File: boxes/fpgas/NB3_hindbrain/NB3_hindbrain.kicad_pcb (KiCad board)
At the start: 2 copper layers, 55.9 x 22.9 mm, 29 parts, among them IC1 FPGA_ICE40UP5K-SG48I, IC2 NOR_Flash_W25Q32JVSSIQ, J1 MicroUSB_10103594-0001LF, J2 Conn_01x20_Male, J3 Conn_01x20_Male, U1 USBtoSPI_FT4232HL, U2 EEPROM_93LC56BT-I-OT, Y1 Osc_12MHz_ECS-2520MV-120-BN-TR

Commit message: NB£_hindbrain layout update
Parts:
- added C12: 100nF, Capacitor_SMD:C_0402_1005Metric, F.Cu at (123.2, 62.2)
- added C13: 4.7uF, Capacitor_SMD:C_0603_1608Metric, F.Cu at (107.0, 66.0)
- added C14: 10uF, Capacitor_SMD:C_0603_1608Metric, F.Cu at (111.1, 66.0)
- added C15: 10uF, Capacitor_SMD:C_0603_1608Metric, F.Cu at (111.1, 63.5)
- added C16: 100nF, Capacitor_SMD:C_0402_1005Metric, F.Cu at (117.4, 65.2)
- added C17: 100nF, Capacitor_SMD:C_0402_1005Metric, F.Cu at (114.5, 67.1)
- added C18: 3.3uF, Capacitor_SMD:C_0603_1608Metric, F.Cu at (107.0, 63.5)
- added C19: 100nF, Capacitor_SMD:C_0402_1005Metric, F.Cu at (114.5, 65.2)
- added C20: 100nF, Capacitor_SMD:C_0402_1005Metric, F.Cu at (120.3, 62.2)
- added C21: 10uF, Capacitor_SMD:C_0603_1608Metric, F.Cu at (115.5, 58.0)
- added C22: 10uF, Capacitor_SMD:C_0603_1608Metric, F.Cu at (115.1, 60.5)
- added C23: 100nF, Capacitor_SMD:C_0402_1005Metric, F.Cu at (121.4, 60.3)
- added C24: 100nF, Capacitor_SMD:C_0402_1005Metric, F.Cu at (117.4, 67.1)
- added C25: 4.7uF, Capacitor_SMD:C_0603_1608Metric, F.Cu at (111.1, 60.9)
- added C26: 100nF, Capacitor_SMD:C_0402_1005Metric, F.Cu at (120.3, 64.2)
- added C27: 4.7uF, Capacitor_SMD:C_0603_1608Metric, F.Cu at (119.5, 58.0)
- added C28: 100nF, Capacitor_SMD:C_0402_1005Metric, F.Cu at (124.3, 59.7)
- added D1: Diode_1N4148WS-7-F, NB3_hindbrain:Diode_1N4148WS-7-F, F.Cu at (107.3, 58.2)
- added FB1: FB_BLM18HE152SN1D, NB3_hindbrain:FB_BLM18HE152SN1D, F.Cu at (111.5, 58.0)
- added FB2: FB_BLM18HE152SN1D, NB3_hindbrain:FB_BLM18HE152SN1D, F.Cu at (107.1, 60.9)
- added R10: 10k, Resistor_SMD:R_0402_1005Metric, F.Cu at (117.4, 62.8)
- added R11: 100, Resistor_SMD:R_0402_1005Metric, F.Cu at (123.0, 57.8)
- added R12: 10k, Resistor_SMD:R_0402_1005Metric, F.Cu at (114.5, 63.2)
- added R9: 10k, Resistor_SMD:R_0402_1005Metric, F.Cu at (118.5, 60.3)
- C1, C2, C8, C9: value 10uF -> 100nF; footprint Capacitor_SMD:C_0603_1608Metric -> Capacitor_SMD:C_0402_1005Metric
- C5: value 100nF -> 4.7uF; footprint Capacitor_SMD:C_0402_1005Metric -> Capacitor_SMD:C_0603_1608Metric
- C7: value 3.3uF -> 100nF; footprint Capacitor_SMD:C_0603_1608Metric -> Capacitor_SMD:C_0402_1005Metric
- R4: value 4.7k -> 10k
- R5: value 10k -> 4.7k
- U1: value USBtoSPI_FT4232HL -> EEPROM_93LC56BT-I-OT; footprint NB3_hindbrain:USBtoSPI_FT4232HL -> NB3_hindbrain:EEPROM_93LC56BT-I-OT
- U2: value EEPROM_93LC56BT-I-OT -> USBtoSPI_FT4232HL; footprint NB3_hindbrain:EEPROM_93LC56BT-I-OT -> NB3_hindbrain:USBtoSPI_FT4232HL
- moved J2 17.8 mm to (133.3, 88.9)
- moved J3 17.8 mm to (133.3, 71.1)
- moved U1 12.5 mm to (104.1, 74.9)
- moved U2 9.67 mm to (94.0, 80.0), turned to 0 degrees
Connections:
- C1 pad 1: +5V -> /FT_VPHY
- C11 pad 2: +3V3 -> +1V8
- C2 pad 1: +5V -> GND
- C2 pad 2: GND -> +3V3
- C3 pad 1: +5V -> GND
- C3 pad 2: GND -> +3V3
- C4 pad 1: +5V -> GND
- C4 pad 2: GND -> +1V8
- C5 pad 1: +1V2 -> /FT_VPHY
- C6 pad 1: +3V3 -> GND
- C6 pad 2: GND -> +3V3
- C7 pad 1: GND -> +3V3
- C7 pad 2: +1V8 -> GND
- C8 pad 1: +1V2 -> GND
- C8 pad 2: GND -> +1V8
- C9 pad 1: +3V3 -> /FT_VPLL
- IC1 pad 1: unconnected-(IC1-Pad1) -> +3V3
- IC1 pad 10: unconnected-(IC1-Pad10) -> /IOB_18A
- IC1 pad 11: unconnected-(IC1-Pad11) -> /IOB_20A
- IC1 pad 12: unconnected-(IC1-Pad12) -> /IOB_22A
- IC1 pad 13: unconnected-(IC1-Pad13) -> /IOB_24A
- IC1 pad 14: /FPGA_SO -> /FLASH_SI
- IC1 pad 15: /FPGA_SCK -> /FLASH_SCK
- IC1 pad 16: /FPGA_SS -> /FLASH_SSn
- IC1 pad 17: /FPGA_SI -> /FLASH_SO
- IC1 pad 18: unconnected-(IC1-Pad18) -> /IOB_31B
- IC1 pad 19: unconnected-(IC1-Pad19) -> /IOB_29B
- IC1 pad 2: unconnected-(IC1-Pad2) -> /IOB_6A
- IC1 pad 20: unconnected-(IC1-Pad20) -> /IOB_25B_G3
- IC1 pad 21: unconnected-(IC1-Pad21) -> /IOB_23B
- IC1 pad 22: unconnected-(IC1-Pad22) -> +3V3
- IC1 pad 23: unconnected-(IC1-Pad23) -> /IOT_37A
- IC1 pad 24: unconnected-(IC1-Pad24) -> Net-(C24-Pad1)
- IC1 pad 25: unconnected-(IC1-Pad25) -> /IOT_36B
- IC1 pad 26: unconnected-(IC1-Pad26) -> /IOT_39A
- IC1 pad 27: unconnected-(IC1-Pad27) -> /IOT_38B
- IC1 pad 28: unconnected-(IC1-Pad28) -> /IOT_41A
- IC1 pad 29: unconnected-(IC1-Pad29) -> Net-(C26-Pad1)
- IC1 pad 3: unconnected-(IC1-Pad3) -> /IOB_9B
- IC1 pad 30: unconnected-(IC1-Pad30) -> +1V2
- IC1 pad 31: unconnected-(IC1-Pad31) -> /IOT_42B
- IC1 pad 32: unconnected-(IC1-Pad32) -> /IOT_43A
- IC1 pad 33: unconnected-(IC1-Pad33) -> +3V3
- IC1 pad 34: unconnected-(IC1-Pad34) -> /IOT_44B
- IC1 pad 35: unconnected-(IC1-Pad35) -> /IOT_46B_G0
- IC1 pad 36: unconnected-(IC1-Pad36) -> /IOT_48B
- IC1 pad 37: unconnected-(IC1-Pad37) -> /IOT_45A_G1
- IC1 pad 38: unconnected-(IC1-Pad38) -> /IOT_50B
- IC1 pad 39: unconnected-(IC1-Pad39) -> /RGB0
- IC1 pad 4: unconnected-(IC1-Pad4) -> /IOB_8A
- IC1 pad 40: unconnected-(IC1-Pad40) -> /RGB1
- IC1 pad 41: unconnected-(IC1-Pad41) -> /RGB2
- IC1 pad 42: unconnected-(IC1-Pad42) -> /IOT_51A
- IC1 pad 43: unconnected-(IC1-Pad43) -> /IOT_49A
- IC1 pad 44: unconnected-(IC1-Pad44) -> /IOB_3B_G6
- IC1 pad 45: unconnected-(IC1-Pad45) -> /IOB_5B
- IC1 pad 46: unconnected-(IC1-Pad46) -> /IOB_0A
- IC1 pad 47: unconnected-(IC1-Pad47) -> /IOB_2A
- IC1 pad 48: unconnected-(IC1-Pad48) -> /IOB_4A
- IC1 pad 49: unconnected-(IC1-Pad49) -> GND
- IC1 pad 5: unconnected-(IC1-Pad5) -> +1V2
- IC1 pad 6: unconnected-(IC1-Pad6) -> /IOB_13B
- IC1 pad 7: unconnected-(IC1-Pad7) -> /CDONE
- IC1 pad 8: unconnected-(IC1-Pad8) -> /CRESET_B
- IC1 pad 9: unconnected-(IC1-Pad9) -> /IOB_16A
- IC2 pad 1: unconnected-(IC2-Pad1) -> /FLASH_SSn
- IC2 pad 2: /FPGA_SI -> /FLASH_SO
- IC2 pad 3: unconnected-(IC2-Pad3) -> /FLASH_WPn
- IC2 pad 5: /FPGA_SO -> /FLASH_SI
- IC2 pad 6: /FPGA_SCK -> /FLASH_SCK
- IC2 pad 7: unconnected-(IC2-Pad7) -> /FLASH_HOLDn
- J2 pad 1: unconnected-(J2-Pad1) -> GND
- J2 pad 10: unconnected-(J2-Pad10) -> /IOB_13B
- J2 pad 11: unconnected-(J2-Pad11) -> /IOB_16A
- J2 pad 12: unconnected-(J2-Pad12) -> /IOB_18A
- J2 pad 13: unconnected-(J2-Pad13) -> /IOB_20A
- J2 pad 14: unconnected-(J2-Pad14) -> /IOB_22A
- J2 pad 15: unconnected-(J2-Pad15) -> /IOB_24A
- J2 pad 16: unconnected-(J2-Pad16) -> /IOB_31B
- J2 pad 17: unconnected-(J2-Pad17) -> /IOB_29B
- J2 pad 18: unconnected-(J2-Pad18) -> /IOB_25B_G3
- J2 pad 19: unconnected-(J2-Pad19) -> /IOB_23B
- J2 pad 2: unconnected-(J2-Pad2) -> /IOB_3B_G6
- J2 pad 20: unconnected-(J2-Pad20) -> GND
- J2 pad 3: unconnected-(J2-Pad3) -> /IOB_5B
- J2 pad 4: unconnected-(J2-Pad4) -> /IOB_0A
- J2 pad 5: unconnected-(J2-Pad5) -> /IOB_2A
- J2 pad 6: unconnected-(J2-Pad6) -> /IOB_4A
- J2 pad 7: unconnected-(J2-Pad7) -> /IOB_6A
- J2 pad 8: unconnected-(J2-Pad8) -> /IOB_9B
- J2 pad 9: unconnected-(J2-Pad9) -> /IOB_8A
- J3 pad 1: unconnected-(J3-Pad1) -> +5V
- J3 pad 10: unconnected-(J3-Pad10) -> /IOT_41A
- J3 pad 11: unconnected-(J3-Pad11) -> /IOT_42B
- J3 pad 12: unconnected-(J3-Pad12) -> /IOT_43A
- J3 pad 13: unconnected-(J3-Pad13) -> /IOT_44B
- J3 pad 14: unconnected-(J3-Pad14) -> /IOT_46B_G0
- J3 pad 15: unconnected-(J3-Pad15) -> /IOT_48B
- J3 pad 16: unconnected-(J3-Pad16) -> /IOT_45A_G1
- J3 pad 17: unconnected-(J3-Pad17) -> /IOT_50B
- J3 pad 18: unconnected-(J3-Pad18) -> /IOT_51A
- J3 pad 19: unconnected-(J3-Pad19) -> /IOT_49A
- J3 pad 2: unconnected-(J3-Pad2) -> +3V3
- J3 pad 20: unconnected-(J3-Pad20) -> +3V3
- J3 pad 3: unconnected-(J3-Pad3) -> /RGB2
- J3 pad 4: unconnected-(J3-Pad4) -> /RGB1
- J3 pad 5: unconnected-(J3-Pad5) -> /RGB0
- J3 pad 6: unconnected-(J3-Pad6) -> /IOT_37A
- J3 pad 7: unconnected-(J3-Pad7) -> /IOT_36B
- J3 pad 8: unconnected-(J3-Pad8) -> /IOT_39A
- J3 pad 9: unconnected-(J3-Pad9) -> /IOT_38B
- R4 pad 1: Net-(J1-Pad1) -> +3V3
- R4 pad 2: Net-(R4-Pad2) -> /EECS
- R5 pad 1: Net-(R4-Pad2) -> Net-(J1-Pad1)
- R5 pad 2: GND -> Net-(R5-Pad2)
- R6 pad 1: +3V3 -> Net-(R5-Pad2)
- R6 pad 2: /EECS -> GND
- R7 pad 1: Net-(R4-Pad2) -> Net-(R5-Pad2)
- U1 pad 1: GND -> /EEDATA_O
- U1 pad 2: /CLK_12MHz -> GND
- U1 pad 3: unconnected-(U1-Pad3) -> /EEDATA_I
- U1 pad 4: unconnected-(U1-Pad4) -> /EECLK
- U1 pad 5: GND -> /EECS
- U1 pad 6: Net-(R8-Pad1) -> +3V3
- U2 pad 1: /EEDATA_O -> GND
- U2 pad 2: GND -> /CLK_12MHz
- U2 pad 3: /EEDATA_I -> unconnected-(U2-Pad3)
- U2 pad 4: /EECLK -> /FT_VPHY
- U2 pad 5: /EECS -> GND
- U2 pad 6: +3V3 -> Net-(R8-Pad1)

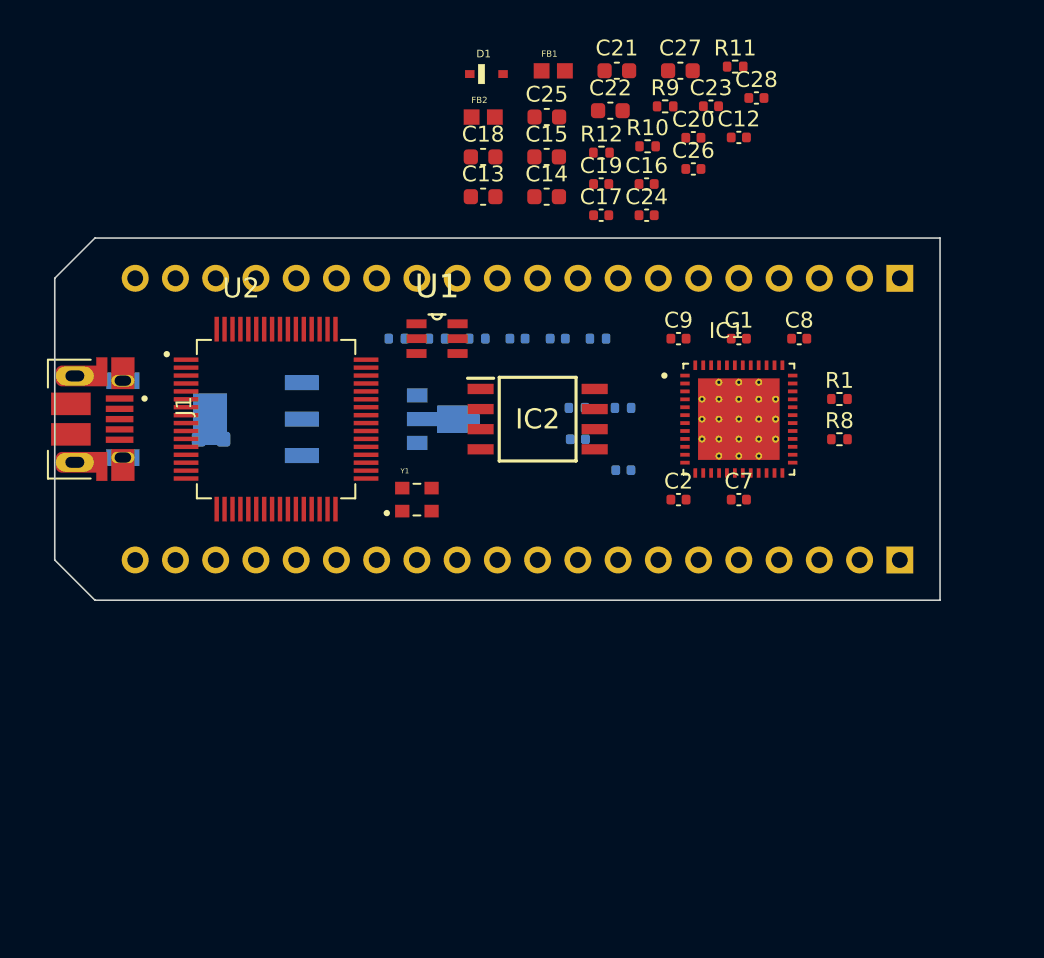
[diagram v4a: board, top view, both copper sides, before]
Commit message: NB£_hindbrain PCB placement done
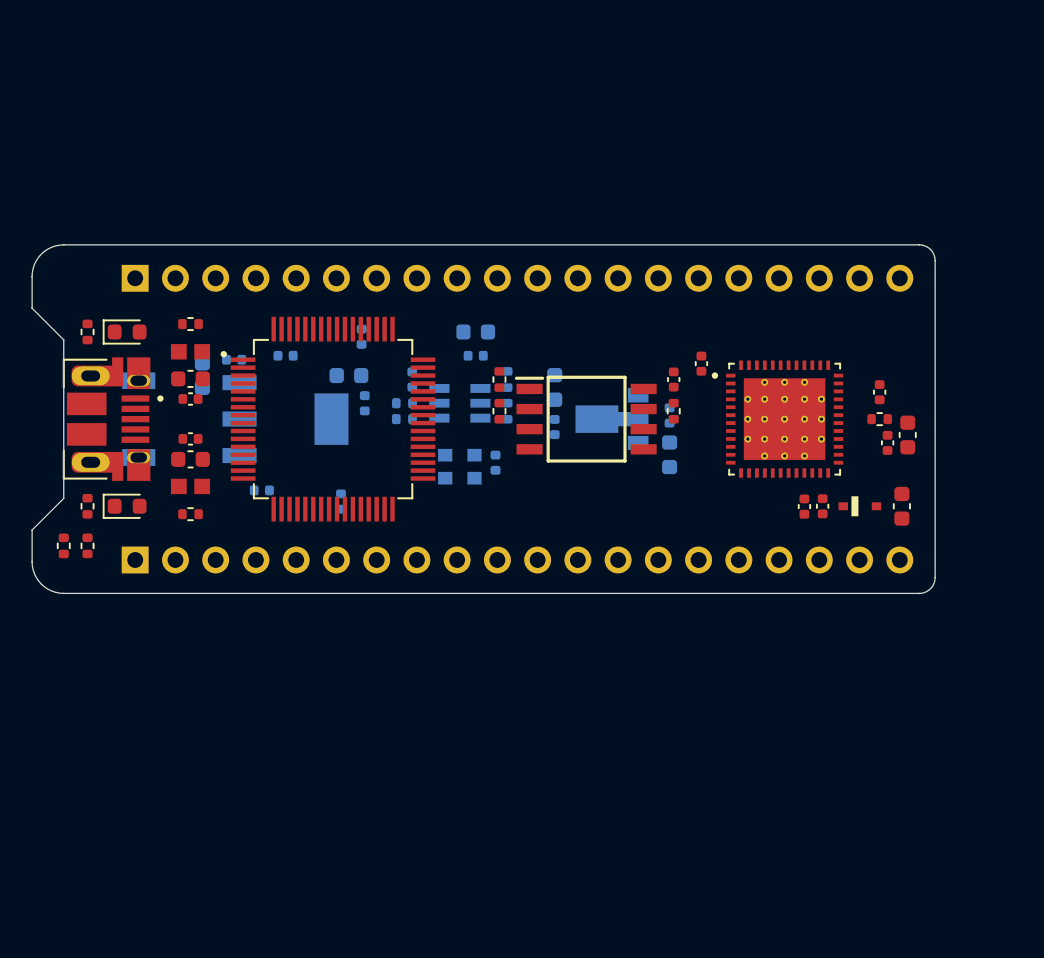
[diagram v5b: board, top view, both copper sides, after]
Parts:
- added D2: Red, LED_SMD:LED_0603_1608Metric, F.Cu at (84.6, 85.5)
- added D3: Diode_1N4148WS-7-F, NB3_hindbrain:Diode_1N4148WS-7-F, F.Cu at (130.8, 85.5)
- added R13: 100, Resistor_SMD:R_0402_1005Metric, F.Cu at (132.1, 80.0)
- added R14: 10k, Resistor_SMD:R_0402_1005Metric, F.Cu at (119.1, 79.5)
- C10, C5, C6, R5, R6, R7: moved to F.Cu
- C14, C15, C16, C17, C18, C19, C2, C20, C21, C22, C28, C7, C8, R1, U1, Y1: moved to B.Cu
- D1: value Diode_1N4148WS-7-F -> Green; footprint NB3_hindbrain:Diode_1N4148WS-7-F -> LED_SMD:LED_0603_1608Metric
- R10: value 10k -> 150
- R11: value 100 -> 10k
- R8: value 12k -> 150
- R9: value 10k -> 12k
- moved J2 48.3 mm to (85.1, 88.9), turned to -90 degrees
- moved J3 48.3 mm to (85.1, 71.1), turned to -90 degrees
- moved R8 47.9 mm to (82.1, 74.5), turned to -90 degrees
- moved R10 42.0 mm to (82.1, 85.5), turned to 90 degrees
- moved C10 38.0 mm to (127.3, 85.5), turned to 90 degrees
- moved FB1 34.8 mm to (88.6, 84.3), turned to 180 degrees
- moved C1 34.8 mm to (88.6, 78.7), turned to 180 degrees
- moved R6 33.5 mm to (80.6, 88.0), turned to 90 degrees
- moved C25 33.3 mm to (133.5, 85.5), turned to -90 degrees
- moved R9 33.0 mm to (88.6, 74.0)
- moved C9 31.4 mm to (88.6, 81.3), turned to 180 degrees
- moved C28 28.3 mm to (107.8, 82.8), turned to 90 degrees
- moved C16 28.3 mm to (91.3, 76.3)
- moved R7 28.0 mm to (88.6, 86.0), turned to 0 degrees
- moved D1 27.9 mm to (84.6, 74.5)
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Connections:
- C15 pad 1: +5V -> +3V3
- C17 pad 1: +5V -> +3V3
- J1 pad 1: Net-(J1-Pad1) -> /USB_5V
- J3 pad 2: +3V3 -> /USB_5V
- R10 pad 1: +3V3 -> Net-(D2-Pad1)
- R10 pad 2: /FLASH_SSn -> GND
- R11 pad 1: +1V2 -> +3V3
- R11 pad 2: Net-(C26-Pad1) -> /FLASH_WPn
- R12 pad 1: /FLASH_HOLDn -> +3V3
- R12 pad 2: +3V3 -> /FLASH_SSn
- R5 pad 1: Net-(J1-Pad1) -> /USB_5V
- R8 pad 1: Net-(R8-Pad1) -> Net-(D1-Pad1)
- R9 pad 1: +3V3 -> Net-(R9-Pad1)
- R9 pad 2: /FLASH_WPn -> GND
- U2 pad 6: Net-(R8-Pad1) -> Net-(R9-Pad1)
- VR2 pad 2: +5V -> +3V3
- VR2 pad 4: +5V -> +3V3
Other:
- board size 55.9 x 22.9 mm -> 57 x 22 mm
- copper layers 2 -> 4

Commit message: NB£_hindbrain routing...work in progress
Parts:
- moved C11 2.71 mm to (92.5, 74.3), turned to 0 degrees
- moved C10 0.50 mm to (127.3, 86.0)
- moved C24 0.50 mm to (128.5, 86.0)
- moved D3 0.50 mm to (130.8, 86.0)
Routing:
- net /USB_DN: track 0.00 -> 6.96 mm
- net /USB_DP: track 0.00 -> 6.90 mm
- net /FT_VPHY: track 0.00 -> 5.81 mm
- net Net-(D1-Pad1): track 0.00 -> 1.92 mm
- net /USB_5V: track 0.00 -> 1.88 mm, vias 0 -> 1
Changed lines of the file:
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@@
   )
   (footprint "Capacitor_SMD:C_0402_1005Metric" (layer "F.Cu")
-    (at 128.48 85.51 -90)
+    (at 128.48 86.01 -90)
     (descr "Capacitor SMD 0402 (1005 Metric), square (rectangular) end terminal, IPC_7351 nominal, (Body size source: IPC-SM-782 page 76, https://www.pcb-3d.com/wordpress/wp-content/uploads/ipc-sm-782a_amendment_1_and_2.pdf), generated with kicad-footprint-generator")
     (tags "capacitor")
@@
   )
   (footprint "Capacitor_SMD:C_0402_1005Metric" (layer "F.Cu")
-    (at 127.33 85.53 90)
+    (at 127.33 86.03 90)
     (descr "Capacitor SMD 0402 (1005 Metric), square (rectangular) end terminal, IPC_7351 nominal, (Body size source: IPC-SM-782 page 76, https://www.pcb-3d.com/wordpress/wp-content/uploads/ipc-sm-782a_amendment_1_and_2.pdf), generated with kicad-footprint-generator")
     (tags "capacitor")
@@
   )
   (footprint "NB3_hindbrain:Diode_1N4148WS-7-F" (layer "F.Cu")
-    (at 130.83 85.51)
+    (at 130.83 86.01)
     (property "MANUFACTURER" "Diodes Inc.")
     (property "Sheetfile" "NB3_hindbrain.kicad_sch")
@@
   )
   (footprint "Capacitor_SMD:C_0402_1005Metric" (layer "B.Cu")
-    (at 94.58 76.01 180)
+    (at 92.455 74.335)
     (descr "Capacitor SMD 0402 (1005 Metric), square (rectangular) end terminal, IPC_7351 nominal, (Body size source: IPC-SM-782 page 76, https://www.pcb-3d.com/wordpress/wp-content/uploads/ipc-sm-782a_amendment_1_and_2.pdf), generated with kicad-footprint-generator")
     (tags "capacitor")
@@
     (fp_line (start 0.5 0.25) (end 0.5 -0.25) (layer "B.Fab") (width 0.1))
     (fp_line (start 0.5 -0.25) (end -0.5 -0.25) (layer "B.Fab") (width 0.1))
-    (pad "1" smd roundrect locked (at -0.48 0 180) (size 0.56 0.62) (layers "B.Cu" "B.Paste" "B.Mask") (roundrect_rratio 0.25)
-      (net 16 "GND") (pintype "passive"))
-    (pad "2" smd roundrect locked (at 0.48 0 180) (size 0.56 0.62) (layers "B.Cu" "B.Paste" "B.Mask") (roundrect_rratio 0.25)
+    (pad "1" smd roundrect locked (at -0.48 0) (size 0.56 0.62) (layers "B.Cu" "B.Paste" "B.Mask") (roundrect_rratio 0.25)
+      (net 16 "GND") (pintype "passive"))
+    (pad "2" smd roundrect locked (at 0.48 0) (size 0.56 0.62) (layers "B.Cu" "B.Paste" "B.Mask") (roundrect_rratio 0.25)
       (net 20 "+1V8") (pintype "passive"))
     (model "${KICAD6_3DMODEL_DIR}/Capacitor_SMD.3dshapes/C_0402_1005Metric.wrl"
@@
   (gr_arc (start 80.58 71.01) (end 80.58 69.01) (angle -90) (layer "Edge.Cuts") (width 0.05))
   (gr_line (start 134.58 91.01) (end 80.58 91.01) (layer "Edge.Cuts") (width 0.05))
+  (segment (start 89.315 75.76) (end 89.315 77.43) (width 0.13) (layer "F.Cu") (net 1))
+  (segment (start 91.9 77.76) (end 90.33 77.76) (width 0.13) (layer "F.Cu") (net 1))
+  (segment (start 89.1 78.74) (end 89.355 78.485) (width 0.13) (layer "F.Cu") (net 1))
+  (segment (start 89.06 78.74) (end 89.1 78.74) (width 0.13) (layer "F.Cu") (net 1))
+  (segment (start 89.315 77.43) (end 89.355 77.47) (width 0.13) (layer "F.Cu") (net 1))
+  (segment (start 89.355 78.485) (end 89.355 77.47) (width 0.13) (layer "F.Cu") (net 1))
+  (segment (start 90.33 77.76) (end 90.04 77.47) (width 0.13) (layer "F.Cu") (net 1))
+  (segment (start 90.04 77.47) (end 89.355 77.47) (width 0.13) (layer "F.Cu") (net 1))
+  (segment (start 87.33 79.51) (end 89.83 79.51) (width 0.13) (layer "F.Cu") (net 13))
+  (segment (start 89.83 79.51) (end 90.08 79.26) (width 0.13) (layer "F.Cu") (net 13))
+  (segment (start 87.18 79.36) (end 87.33 79.51) (width 0.13) (layer "F.Cu") (net 13))
+  (segment (start 85.105 79.36) (end 87.18 79.36) (width 0.13) (layer "F.Cu") (net 13))
+  (segment (start 90.08 79.26) (end 91.9 79.26) (width 0.13) (layer "F.Cu") (net 13))
+  (segment (start 89.866722 80.01) (end 90.116722 79.76) (width 0.13) (layer "F.Cu") (net 14))
+  (segment (start 90.116722 79.76) (end 91.9 79.76) (width 0.13) (layer "F.Cu") (net 14))
+  (segment (start 85.105 80.01) (end 89.866722 80.01) (width 0.13) (layer "F.Cu") (net 14))
+  (segment (start 85.105 78.71) (end 86.98 78.71) (width 0.13) (layer "F.Cu") (net 65))
+  (via (at 86.98 78.71) (size 0.45) (drill 0.25) (layers "F.Cu" "B.Cu") (net 65))
+  (segment (start 82.08 74) (end 83.2825 74) (width 0.13) (layer "F.Cu") (net 87))
+  (segment (start 83.2825 74) (end 83.7925 74.51) (width 0.13) (layer "F.Cu") (net 87))
 )

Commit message: Tweaks to NB3_hindbrain
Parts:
- removed U2: USBtoSPI_FT4232HL, NB3_hindbrain:USBtoSPI_FT4232HL
- added IC3: FT232HL, NB3_hindbrain:USBtoSPI_FT232HL, F.Cu at (96.6, 79.8)
- added IC4: ADC_MCP3004-I-SL, NB3_hindbrain:ADC_MCP3004-I-SL, B.Cu at (129.9, 79.8)
- D1: value Green -> LED
- D2: value Red -> LED
- moved IC2 0.91 mm to (113.6, 79.1)
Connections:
- D2 pad 2: /USB_5V -> +5V
- FB1 pad 2: +3V3 -> Net-(FB1-Pad2)
- FB2 pad 2: +3V3 -> Net-(FB1-Pad2)
- R7 pad 2: Net-(R7-Pad2) -> unconnected-(R7-Pad2)
- R9 pad 1: Net-(R9-Pad1) -> unconnected-(R9-Pad1)
